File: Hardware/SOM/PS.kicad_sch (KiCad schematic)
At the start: 1 part, among them U3 TLV62569DBV

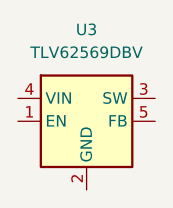
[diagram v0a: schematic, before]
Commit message: QSPI, banks IO decoupling
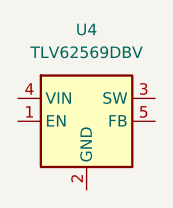
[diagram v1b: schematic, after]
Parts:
- renumbered U3 to U4
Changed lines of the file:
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@@
 		(dnp no)
 		(fields_autoplaced yes)
-		(property "Reference" "U3"
+		(property "Reference" "U4"
 			(at 146.05 106.68 0)
 			(effects
@@
 			(project "LFE5UM5G-85F_SOM"
 				(path "/de32abb0-ff3b-4c67-a91a-eed08140b1b2/c12b65b4-6107-4b66-8aa5-205f87459293"
-					(reference "U3")
+					(reference "U4")
 					(unit 1)
 				)

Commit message: SOM: power supplies
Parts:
- removed U4: TLV62569DBV, Package_TO_SOT_SMD:SOT-23-5, symbol Regulator_Switching:TLV62569DBV
- added C75, C76, C77, C78: 22uF, Capacitor_SMD:C_0805_2012Metric, symbol RA8M1:885012205092
- added C79, C80, C81, C82: 10uF, Capacitor_SMD:C_0402_1005Metric, symbol RA8M1:885012205092
- added L1, L2, L3, L4: 1uH, symbol Device:L
- added R27: 442k, Resistor_SMD:R_0402_1005Metric, symbol Device:R
- added R28, R30, R32, R33, R34: 100K, Resistor_SMD:R_0402_1005Metric, symbol Device:R
- added R29: 316k, Resistor_SMD:R_0402_1005Metric, symbol Device:R
- added R31: 150k, Resistor_SMD:R_0402_1005Metric, symbol Device:R
- added U4, U5, U6, U7: TPS62A02ADRL, Package_TO_SOT_SMD:SOT-563, symbol Regulator_Switching:TPS62A02ADRL
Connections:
- new net: R33.1, R34.2, U7.5 (FB)
- new net: L4.1, U7.2 (SW)
- new net: L1.1, U5.2 (SW)
- new net: R27.1, R28.2, U5.5 (FB)
- new net: L3.1, U6.2 (SW)
- new net: L2.1, U4.2 (SW)
- new net: R29.1, R30.2, U4.5 (FB)
- new net: R31.1, R32.2, U6.5 (FB)
- new net 1.2V: C77.2, L4.2, R33.2
- new net 1.5V: C75.2, L3.2, R31.2
- new net 2.5V: C78.2, L2.2, R29.2
- new net 3.3V: C76.2, L1.2, R27.2
- new net 5V: C79.2, C80.2, C81.2, C82.2, U4.3 (VIN), U5.3 (VIN), U6.3 (VIN), U7.3 (VIN)
- new net GND: C75.1, C76.1, C77.1, C78.1, C79.1, C80.1, C81.1, C82.1, R28.1, R30.1, R32.1, R34.1, U4.1 (GND), U5.1 (GND), U6.1 (GND), U7.1 (GND)
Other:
- note added: "1.8A"
- note added: "PS 1.2V"
- note added: "PS 1.5V"
- note added: "PS 2.5V"
- note added: "PS 3.3V"
- note added: "R1=100k((1.2V/0.6V)-1)=100k"
- note added: "R1=100k((1.5V/0.6V)-1)=150k"
- note added: "R1=100k((2.5V/0.6V)-1)=317k"
- note added: "R1=100k((3.3V/0.6V)-1)=450k"

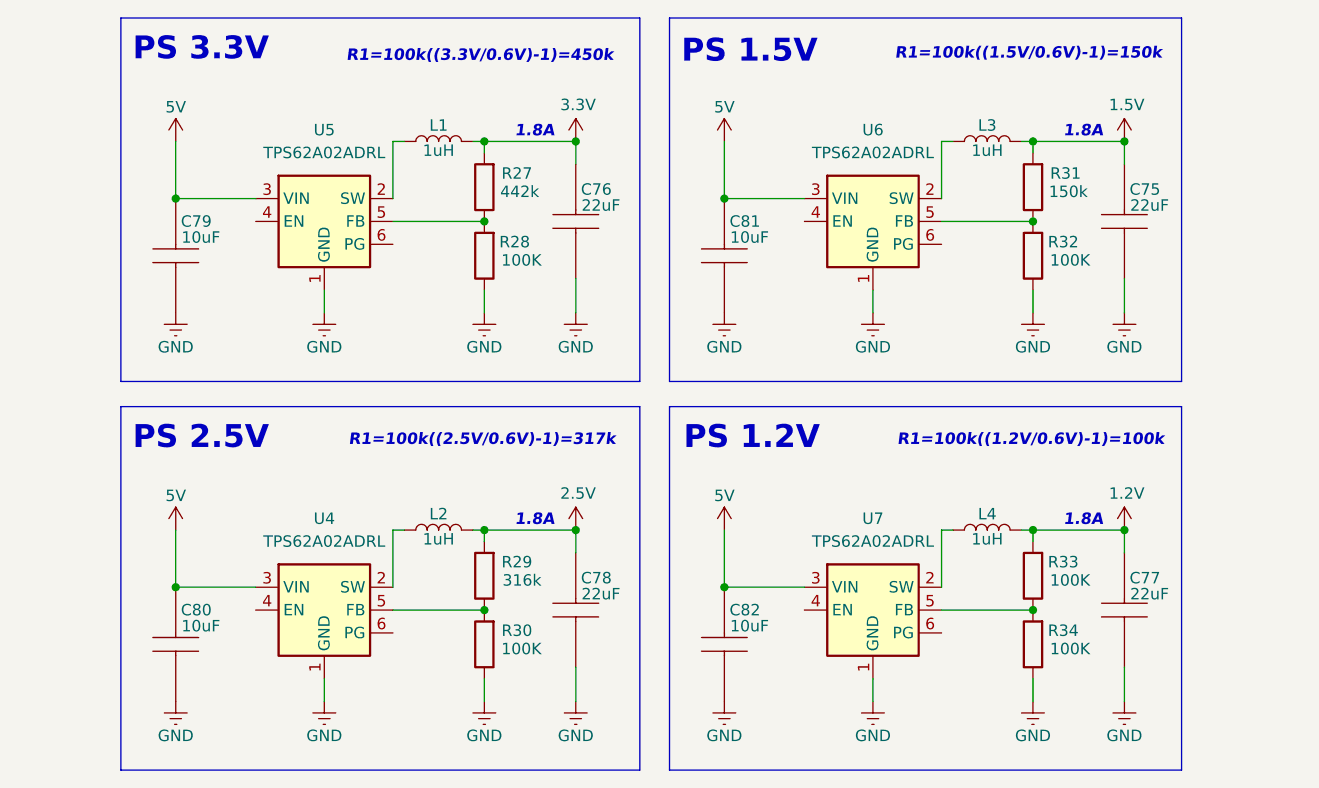
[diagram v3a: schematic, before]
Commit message: SOM: power supply update
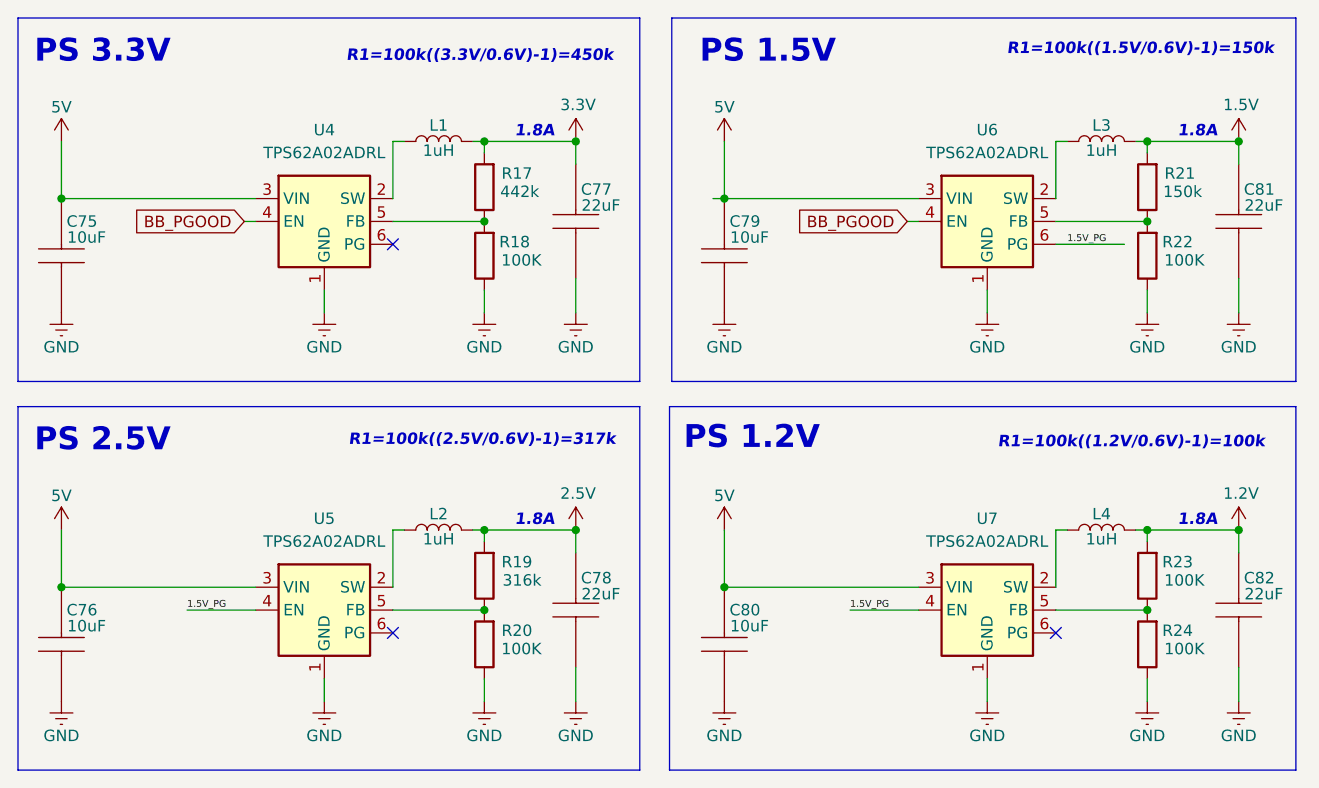
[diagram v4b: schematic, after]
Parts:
- L1, L2, L3, L4: footprint (none) -> Inductor_SMD:L_0805_2012Metric
- renumbered C79 to C75, C80 to C76, C76 to C77, C81 to C79, C82 to C80, C75 to C81, C77 to C82, R27 to R17, R28 to R18, R29 to R19, R30 to R20, R31 to R21, R32 to R22, R33 to R23, R34 to R24, U5 to U4, U4 to U5
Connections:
- net 1.5V_PG: now reaches U7.4 (EN)
- net 1.5V_PG: now also U5.4 (EN), U6.6 (PG)
- net BB_PGOOD: now reaches U4.4 (EN)
- net BB_PGOOD: now also U6.4 (EN)
- no-connect marks 0 -> 3
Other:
- moved on the sheet: C75, C76, C81, C82, L3, L4, R21, R22, R23, R24, U6, U7

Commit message: SOM: layout update
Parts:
- renumbered C80 to C100, C81 to C101, C82 to C102, C75 to C95, C76 to C96, C77 to C97, C78 to C98, C79 to C99
